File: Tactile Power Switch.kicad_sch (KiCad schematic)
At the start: 12 parts, among them J1 OSTTC020162, J2 OSTTC020162, Q1 BC847B_215, Q2 BC847B_215, Q3 DMG2305UX-13

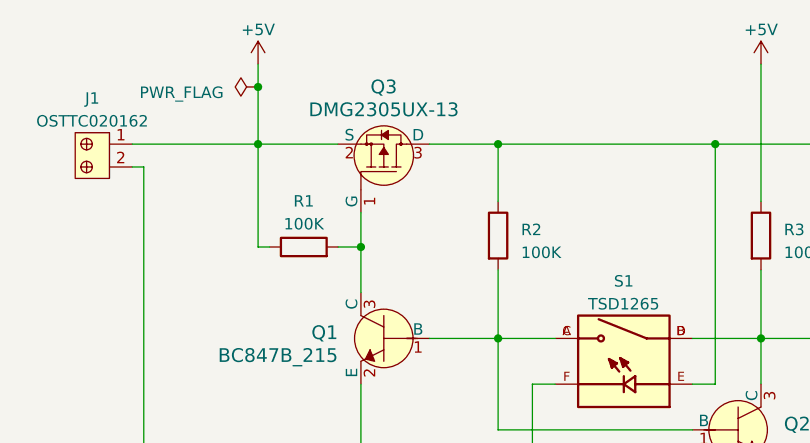
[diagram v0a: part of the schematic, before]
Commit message: Schmatics after final component selection
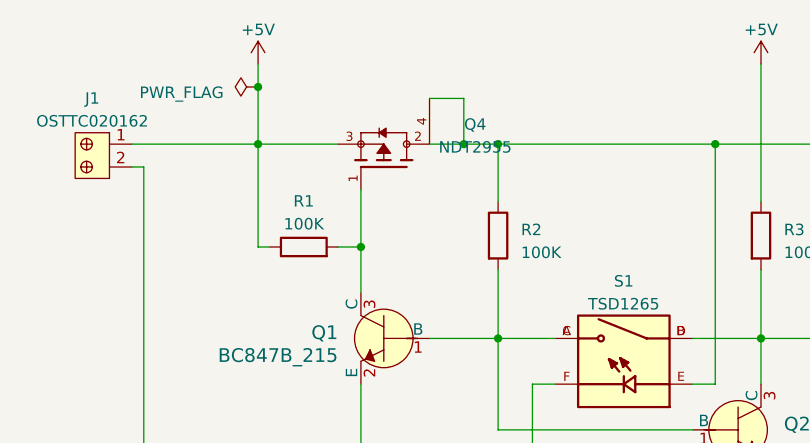
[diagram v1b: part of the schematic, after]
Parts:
- removed Q3: DMG2305UX-13, digikey-footprints:SOT-23-3, symbol dk_Transistors-FETs-MOSFETs-Single:DMG2305UX-13
- added Q4: NDT2955, MOSFET:SOT223, symbol NDT2955:NDT2955
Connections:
- net +5V: now also Q4.3
- net VDD: now also Q4.2, Q4.4
- net at Q1.3 (C), R1.2: now also Q4.1
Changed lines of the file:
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@@
   (junction (at 158.75 92.71) (diameter 0) (color 0 0 0 0)
   )
+  (junction (at 125.73 71.12) (diameter 0) (color 0 0 0 0)
+  )
   (junction (at 114.3 82.55) (diameter 0) (color 0 0 0 0)
   )
@@
     (stroke (width 0) (type default))
   )
+  (wire (pts (xy 121.92 66.04) (xy 125.73 66.04))
+    (stroke (width 0) (type default))
+  )
   (wire (pts (xy 133.35 113.03) (xy 133.35 114.3))
     (stroke (width 0) (type default))
@@
     (stroke (width 0) (type default))
   )
+  (wire (pts (xy 125.73 71.12) (xy 129.54 71.12))
+    (stroke (width 0) (type default))
+  )
+  (wire (pts (xy 125.73 66.04) (xy 125.73 71.12))
+    (stroke (width 0) (type default))
+  )
   (wire (pts (xy 151.13 92.71) (xy 158.75 92.71))
     (stroke (width 0) (type default))
@@
     (stroke (width 0) (type default))
   )
-  (wire (pts (xy 114.3 78.74) (xy 114.3 82.55))
+  (wire (pts (xy 114.3 76.2) (xy 114.3 82.55))
     (stroke (width 0) (type default))
   )
@@
     (stroke (width 0) (type default))
   )
-  (wire (pts (xy 121.92 71.12) (xy 129.54 71.12))
+  (wire (pts (xy 121.92 71.12) (xy 125.73 71.12))
     (stroke (width 0) (type default))
   )
@@
     )
   )
-  (symbol (lib_id "dk_Transistors-FETs-MOSFETs-Single:DMG2305UX-13") (at 116.84 71.12 270) (mirror x) (unit 1)
-    (in_bom yes) (on_board yes) (dnp no)
-    (property "Reference" "Q3" (at 116.84 64.77 90)
-      (effects (font (size 1.524 1.524)))
-    )
-    (property "Value" "DMG2305UX-13" (at 116.84 67.31 90)
-      (effects (font (size 1.524 1.524)))
-    )
-    (property "Footprint" "digikey-footprints:SOT-23-3" (at 121.92 66.04 0)
-      (effects (font (size 1.524 1.524)) (justify left) hide)
-    )
-    (property "Datasheet" "https://www.diodes.com/assets/Datasheets/DMG2305UX.pdf" (at 124.46 66.04 0)
-      (effects (font (size 1.524 1.524)) (justify left) hide)
-    )
-    (property "Digi-Key_PN" "DMG2305UX-13DICT-ND" (at 127 66.04 0)
-      (effects (font (size 1.524 1.524)) (justify left) hide)
-    )
-    (property "MPN" "DMG2305UX-13" (at 129.54 66.04 0)
-      (effects (font (size 1.524 1.524)) (justify left) hide)
-    )
-    (property "Category" "Discrete Semiconductor Products" (at 132.08 66.04 0)
-      (effects (font (size 1.524 1.524)) (justify left) hide)
-    )
-    (property "Family" "Transistors - FETs, MOSFETs - Single" (at 134.62 66.04 0)
-      (effects (font (size 1.524 1.524)) (justify left) hide)
-    )
-    (property "DK_Datasheet_Link" "https://www.diodes.com/assets/Datasheets/DMG2305UX.pdf" (at 137.16 66.04 0)
-      (effects (font (size 1.524 1.524)) (justify left) hide)
-    )
-    (property "DK_Detail_Page" "/product-detail/en/diodes-incorporated/DMG2305UX-13/DMG2305UX-13DICT-ND/4251589" (at 139.7 66.04 0)
-      (effects (font (size 1.524 1.524)) (justify left) hide)
-    )
-    (property "Description" "MOSFET P-CH 20V 4.2A SOT23" (at 142.24 66.04 0)
-      (effects (font (size 1.524 1.524)) (justify left) hide)
-    )
-    (property "Manufacturer" "Diodes Incorporated" (at 144.78 66.04 0)
-      (effects (font (size 1.524 1.524)) (justify left) hide)
-    )
-    (property "Status" "Active" (at 147.32 66.04 0)
-      (effects (font (size 1.524 1.524)) (justify left) hide)
-    )
-    (pin "1")
-    (pin "2")
-    (pin "3")
-    (instances
-      (project "Tactile Power Switch"
-        (path "/72a9c836-61c4-4172-ab46-eebab5956cc2"
-          (reference "Q3") (unit 1)
-        )
-      )
-    )
-  )
   (symbol (lib_id "dk_Terminal-Blocks-Wire-to-Board:OSTTC020162") (at 83.82 71.12 270) (unit 1)
     (in_bom yes) (on_board yes) (dnp no) (fields_autoplaced)
@@
         )
       )
+    )
+  )
+  (symbol (lib_id "NDT2955:NDT2955") (at 116.84 73.66 90) (unit 1)
+    (in_bom yes) (on_board yes) (dnp no) (fields_autoplaced)
+    (property "Reference" "Q4" (at 127 68.9357 90)
+      (effects (font (size 1.27 1.27)))
+    )
+    (property "Value" "NDT2955" (at 127 71.4757 90)
+      (effects (font (size 1.27 1.27)))
+    )
+    (property "Footprint" "MOSFET:SOT223" (at 116.84 73.66 0)
+      (effects (font (size 1.27 1.27)) (justify bottom) hide)
+    )
+    (property "Datasheet" "" (at 116.84 73.66 0)
+      (effects (font (size 1.27 1.27)) hide)
+    )
+    (property "MF" "ON Semiconductor" (at 116.84 73.66 0)
+      (effects (font (size 1.27 1.27)) (justify bottom) hide)
+    )
+    (property "Description" "\nP-Channel 60 V 2.5A (Ta) 3W (Ta) Surface Mount SOT-223-4\n" (at 116.84 73.66 0)
+      (effects (font (size 1.27 1.27)) (justify bottom) hide)
+    )
+    (property "Package" "SOT-223-4 Rochester Electronics" (at 116.84 73.66 0)
+      (effects (font (size 1.27 1.27)) (justify bottom) hide)
+    )
+    (property "Price" "None" (at 116.84 73.66 0)
+      (effects (font (size 1.27 1.27)) (justify bottom) hide)
+    )
+    (property "SnapEDA_Link" "https://www.snapeda.com/parts/NDT2955/Onsemi/view-part/?ref=snap" (at 116.84 73.66 0)
+      (effects (font (size 1.27 1.27)) (justify bottom) hide)
+    )
+    (property "MP" "NDT2955" (at 116.84 73.66 0)
+      (effects (font (size 1.27 1.27)) (justify bottom) hide)
+    )
+    (property "Purchase-URL" "https://www.snapeda.com/api/url_track_click_mouser/?unipart_id=1238638&manufacturer=ON Semiconductor&part_name=NDT2955&search_term=None" (at 116.84 73.66 0)
+      (effects (font (size 1.27 1.27)) (justify bottom) hide)
+    )
+    (property "Availability" "In Stock" (at 116.84 73.66 0)
+      (effects (font (size 1.27 1.27)) (justify bottom) hide)
+    )
+    (property "Check_prices" "https://www.snapeda.com/parts/NDT2955/Onsemi/view-part/?ref=eda" (at 116.84 73.66 0)
+      (effects (font (size 1.27 1.27)) (justify bottom) hide)
+    )
+    (pin "1")
+    (pin "2")
+    (pin "3")
+    (pin "4")
+    (instances
+      (project "Tactile Power Switch"
+        (path "/72a9c836-61c4-4172-ab46-eebab5956cc2"
+          (reference "Q4") (unit 1)
+        )
+      )

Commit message: Placement Finished
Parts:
- added H1, H2: MountingHole, MountingHole:MountingHole_2.7mm_M2.5_ISO7380, symbol Mechanical:MountingHole
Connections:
- net +5V renamed +12V

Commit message: Palcement Change, Screw Terminal footfrint change to 2.54 inch and overall pcb outline optimization
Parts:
- J1, J2: footprint Screw_Terminal:Screw_Terminal-2_pins -> TerminalBlock:TerminalBlock_Xinya_XY308-2.54-2P_1x02_P2.54mm_Horizontal
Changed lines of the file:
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@@
 			)
 		)
-		(property "Footprint" "Screw_Terminal:Screw_Terminal-2_pins"
+		(property "Footprint" "TerminalBlock:TerminalBlock_Xinya_XY308-2.54-2P_1x02_P2.54mm_Horizontal"
 			(at 88.9 76.2 0)
 			(effects
@@
 			)
 		)
-		(property "Footprint" "Screw_Terminal:Screw_Terminal-2_pins"
+		(property "Footprint" "TerminalBlock:TerminalBlock_Xinya_XY308-2.54-2P_1x02_P2.54mm_Horizontal"
 			(at 190.5 68.58 0)
 			(effects

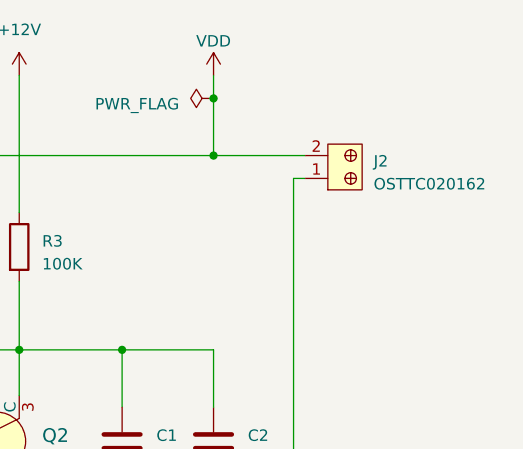
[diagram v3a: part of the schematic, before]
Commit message: Terminal output connector configureation change
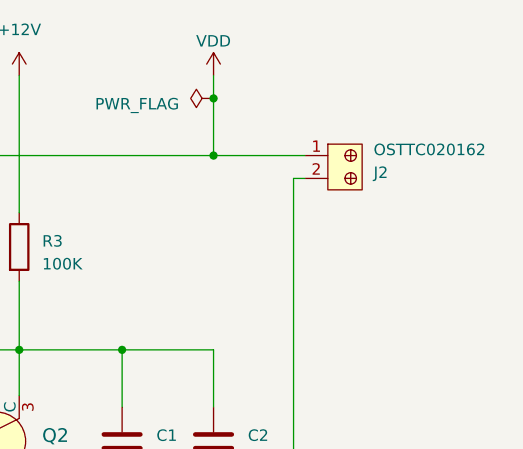
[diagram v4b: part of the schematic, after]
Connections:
- net GND: now also J2.2; no longer J2.1
- net VDD: now also J2.1; no longer J2.2
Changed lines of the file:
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@@
 	(symbol
 		(lib_id "dk_Terminal-Blocks-Wire-to-Board:OSTTC020162")
-		(at 195.58 73.66 90)
+		(at 195.58 71.12 90)
+		(mirror x)
 		(unit 1)
 		(exclude_from_sim no)
@@
 		(on_board yes)
 		(dnp no)
-		(fields_autoplaced yes)
 		(property "Reference" "J2"
-			(at 198.12 71.755 90)
+			(at 198.12 73.025 90)
 			(effects
 				(font
@@
 		)
 		(property "Value" "OSTTC020162"
-			(at 198.12 74.295 90)
+			(at 198.12 70.485 90)
 			(effects
 				(font
@@
 		)
 		(property "Footprint" "TerminalBlock:TerminalBlock_Xinya_XY308-2.54-2P_1x02_P2.54mm_Horizontal"
-			(at 190.5 68.58 0)
+			(at 190.5 76.2 0)
 			(effects
 				(font
@@
 		)
 		(property "Datasheet" "http://www.on-shore.com/wp-content/uploads/OSTTCXX0162.pdf"
-			(at 187.96 68.58 0)
+			(at 187.96 76.2 0)
 			(effects
 				(font
@@
 		)
 		(property "Description" "TERM BLK 2POS SIDE ENTRY 5MM PCB"
-			(at 170.18 68.58 0)
+			(at 170.18 76.2 0)
 			(effects
 				(font
@@
 		)
 		(property "Digi-Key_PN" "ED2600-ND"
-			(at 185.42 68.58 0)
+			(at 185.42 76.2 0)
 			(effects
 				(font
@@
 		)
 		(property "MPN" "OSTTC020162"
-			(at 182.88 68.58 0)
+			(at 182.88 76.2 0)
 			(effects
 				(font
@@
 		)
 		(property "Category" "Connectors, Interconnects"
-			(at 180.34 68.58 0)
+			(at 180.34 76.2 0)
 			(effects
 				(font
@@
 		)
 		(property "Family" "Terminal Blocks - Wire to Board"
-			(at 177.8 68.58 0)
+			(at 177.8 76.2 0)
 			(effects
 				(font
@@
 		)
 		(property "DK_Datasheet_Link" "http://www.on-shore.com/wp-content/uploads/OSTTCXX0162.pdf"
-			(at 175.26 68.58 0)
+			(at 175.26 76.2 0)
 			(effects
 				(font
@@
 		)
 		(property "DK_Detail_Page" "/product-detail/en/on-shore-technology-inc/OSTTC020162/ED2600-ND/614549"
-			(at 172.72 68.58 0)
+			(at 172.72 76.2 0)
 			(effects
 				(font
@@
 		)
 		(property "Manufacturer" "On Shore Technology Inc."
-			(at 167.64 68.58 0)
+			(at 167.64 76.2 0)
 			(effects
 				(font
@@
 		)
 		(property "Status" "Active"
-			(at 165.1 68.58 0)
+			(at 165.1 76.2 0)
 			(effects
 				(font

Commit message: MOSFET footprint update, Silkscreen update
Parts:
- Q4: footprint MOSFET:SOT223 -> Package_TO_SOT_SMD:SOT-223
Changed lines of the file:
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@@
 			)
 		)
-		(property "Footprint" "MOSFET:SOT223"
+		(property "Footprint" "Package_TO_SOT_SMD:SOT-223"
 			(at 116.84 73.66 0)
 			(effects
@@
 			)
 		)
-		(property "Description" "\nP-Channel 60 V 2.5A (Ta) 3W (Ta) Surface Mount SOT-223-4\n"
+		(property "Description" "P-Channel 60 V 2.5A (Ta) 3W (Ta) Surface Mount SOT-223-4"
 			(at 116.84 73.66 0)
 			(effects

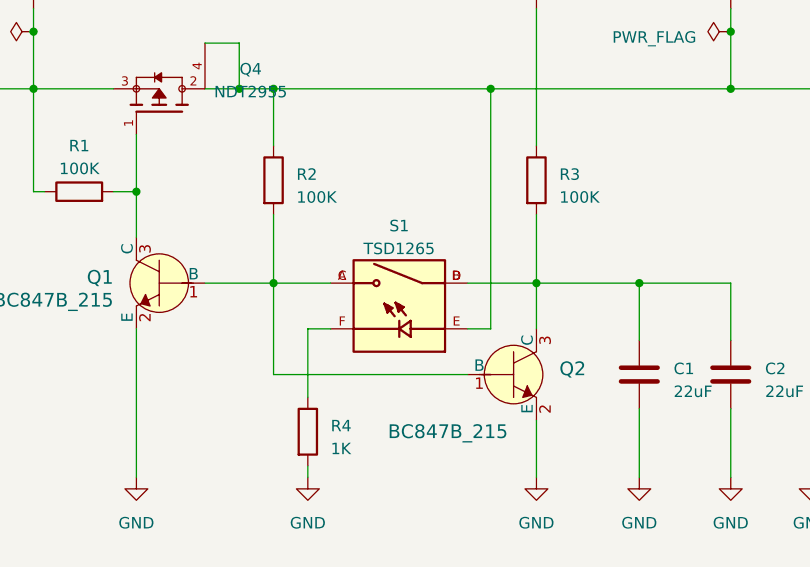
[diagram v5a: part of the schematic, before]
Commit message: smd version restored + mfg file created
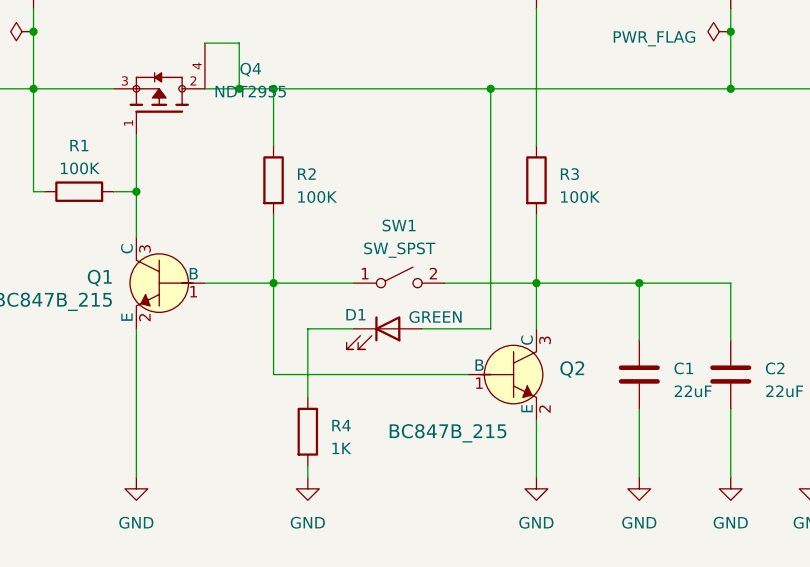
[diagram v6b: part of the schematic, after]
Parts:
- removed S1: TSD1265, SW_TSD1265:SW_TSD1265, symbol TSD1265:TSD1265
- added D1: GREEN, LED_SMD:LED_0603_1608Metric, symbol Device:LED
- added SW1: SW_SPST, Button_Switch_SMD:SW_SPST_TL3342, symbol Switch:SW_SPST
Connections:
- net VDD: now also D1.2 (A)
- net at Q1.1 (B), Q2.1 (B), R2.2: now also SW1.1 (A)
- net at C1.1, C2.1, Q2.3 (C)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: now also SW1.2 (B)
- net at R4.1: now also D1.1 (K)
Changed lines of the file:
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@@
 	(wire
 		(pts
-			(xy 153.67 97.79) (xy 151.13 97.79)
+			(xy 153.67 97.79) (xy 146.05 97.79)
 		)
 		(stroke
@@
 	(wire
 		(pts
-			(xy 151.13 92.71) (xy 158.75 92.71)
+			(xy 148.59 92.71) (xy 158.75 92.71)
 		)
 		(stroke
@@
 	(wire
 		(pts
-			(xy 129.54 92.71) (xy 135.89 92.71)
+			(xy 129.54 92.71) (xy 138.43 92.71)
 		)
 		(stroke
@@
 	(wire
 		(pts
-			(xy 133.35 97.79) (xy 135.89 97.79)
+			(xy 133.35 97.79) (xy 138.43 97.79)
 		)
 		(stroke
@@
 	)
 	(symbol
-		(lib_id "TSD1265:TSD1265")
-		(at 143.51 95.25 0)
-		(mirror y)
+		(lib_id "Switch:SW_SPST")
+		(at 143.51 92.71 0)
 		(unit 1)
 		(exclude_from_sim no)
@@
 		(on_board yes)
 		(dnp no)
-		(property "Reference" "S1"
+		(fields_autoplaced yes)
+		(property "Reference" "SW1"
 			(at 143.51 86.36 0)
 			(effects
@@
 			)
 		)
-		(property "Value" "TSD1265"
+		(property "Value" "SW_SPST"
 			(at 143.51 88.9 0)
 			(effects
@@
 			)
 		)
-		(property "Footprint" "SW_TSD1265:SW_TSD1265"
-			(at 143.51 95.25 0)
-			(effects
-				(font
-					(size 1.27 1.27)
-				)
-				(justify bottom)
-				(hide yes)
-			)
-		)
-		(property "Datasheet" ""
-			(at 143.51 95.25 0)
-			(effects
-				(font
-					(size 1.27 1.27)
-				)
-				(hide yes)
-			)
-		)
-		(property "Description" "\nTactile Push Button Switch Momentary\n"
-			(at 143.51 95.25 0)
-			(effects
-				(font
-					(size 1.27 1.27)
-				)
-				(justify bottom)
-				(hide yes)
-			)
-		)
-		(property "MF" "Omten Electronics"
-			(at 143.51 95.25 0)
-			(effects
-				(font
-					(size 1.27 1.27)
-				)
-				(justify bottom)
-				(hide yes)
-			)
-		)
-		(property "MAXIMUM_PACKAGE_HEIGHT" "6.5 mm"
-			(at 143.51 95.25 0)
-			(effects
-				(font
-					(size 1.27 1.27)
-				)
-				(justify bottom)
-				(hide yes)
-			)
-		)
-		(property "Package" "Package"
-			(at 143.51 95.25 0)
-			(effects
-				(font
-					(size 1.27 1.27)
-				)
-				(justify bottom)
-				(hide yes)
-			)
-		)
-		(property "Price" "None"
-			(at 143.51 95.25 0)
-			(effects
-				(font
-					(size 1.27 1.27)
-				)
-				(justify bottom)
-				(hide yes)
-			)
-		)
-		(property "Check_prices" "https://www.snapeda.com/parts/TSD1265/Omten+Electronics/view-part/?ref=eda"
-			(at 143.51 95.25 0)
-			(effects
-				(font
-					(size 1.27 1.27)
-				)
-				(justify bottom)
-				(hide yes)
-			)
-		)
-		(property "STANDARD" "Manufacturer Recommendations"
-			(at 143.51 95.25 0)
-			(effects
-				(font
-					(size 1.27 1.27)
-				)
-				(justify bottom)
-				(hide yes)
-			)
-		)
-		(property "PARTREV" "N/A"
-			(at 143.51 95.25 0)
-			(effects
-				(font
-					(size 1.27 1.27)
-				)
-				(justify bottom)
-				(hide yes)
-			)
-		)
-		(property "SnapEDA_Link" "https://www.snapeda.com/parts/TSD1265/Omten+Electronics/view-part/?ref=snap"
-			(at 143.51 95.25 0)
-			(effects
-				(font
-					(size 1.27 1.27)
-				)
-				(justify bottom)
-				(hide yes)
-			)
-		)
-		(property "MP" "TSD1265"
-			(at 143.51 95.25 0)
-			(effects
-				(font
-					(size 1.27 1.27)
-				)
-				(justify bottom)
-				(hide yes)
-			)
-		)
-		(property "Availability" "Not in stock"
-			(at 143.51 95.25 0)
-			(effects
-				(font
-					(size 1.27 1.27)
-				)
-				(justify bottom)
-				(hide yes)
-			)
-		)
-		(property "MANUFACTURER" "Omten Electronics"
-			(at 143.51 95.25 0)
-			(effects
-				(font
-					(size 1.27 1.27)
-				)
-				(justify bottom)
-				(hide yes)
-			)
-		)
-		(pin "A"
-		)
-		(pin "B"
-		)
-		(pin "C"
-		)
-		(pin "D"
-		)
-		(pin "E"
-		)
-		(pin "F"
+		(property "Footprint" "Button_Switch_SMD:SW_SPST_TL3342"
+			(at 143.51 92.71 0)
+			(effects
+				(font
+					(size 1.27 1.27)
+				)
+				(hide yes)
+			)
+		)
+		(property "Datasheet" "~"
+			(at 143.51 92.71 0)
+			(effects
+				(font
+					(size 1.27 1.27)
+				)
+				(hide yes)
+			)
+		)
+		(property "Description" "Single Pole Single Throw (SPST) switch"
+			(at 143.51 92.71 0)
+			(effects
+				(font
+					(size 1.27 1.27)
+				)
+				(hide yes)
+			)
+		)
+		(pin "1"
+		)
+		(pin "2"
 		)
 		(instances
-			(project "Tactile Power Switch"
+			(project ""
 				(path "/72a9c836-61c4-4172-ab46-eebab5956cc2"
-					(reference "S1")
+					(reference "SW1")
 					(unit 1)
 				)
@@
 					(unit 1)
 				)
+			)
+		)
+	)
+	(symbol
+		(lib_id "Device:LED")
+		(at 142.24 97.79 0)
+		(unit 1)
+		(exclude_from_sim no)
+		(in_bom yes)
+		(on_board yes)
+		(dnp no)
+		(property "Reference" "D1"
+			(at 138.684 96.266 0)
+			(effects
+				(font
+					(size 1.27 1.27)
+				)
+			)
+		)
+		(property "Value" "GREEN"
+			(at 147.574 96.52 0)
+			(effects
+				(font
+					(size 1.27 1.27)
+				)
+			)
+		)
+		(property "Footprint" "LED_SMD:LED_0603_1608Metric"
+			(at 142.24 97.79 0)
+			(effects
+				(font
+					(size 1.27 1.27)
+				)
+				(hide yes)
+			)
+		)
+		(property "Datasheet" "~"
+			(at 142.24 97.79 0)
+			(effects
+				(font
+					(size 1.27 1.27)
+				)
+				(hide yes)
+			)
+		)
+		(property "Description" "Light emitting diode"
+			(at 142.24 97.79 0)
+			(effects
+				(font
+					(size 1.27 1.27)
+				)
+				(hide yes)
+			)
+		)
+		(pin "1"
+		)
+		(pin "2"
+		)
+		(instances
+			(project ""
+				(path "/72a9c836-61c4-4172-ab46-eebab5956cc2"
+					(reference "D1")
+					(unit 1)
+				)
